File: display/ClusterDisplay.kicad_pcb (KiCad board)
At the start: 4 copper layers, 105 x 106 mm, 76 parts, among them J1 Verdin iMX95, J10 RTC coin cell, J2 Power in, J3 CAN to ECU, J4 DM-TFTR50-413 panel, J8 JTAG debug, J9 Buttons, Q1 NFET diode, Q2 NFET pass, Q3 MFT6N2A5S23A (AEC-Q101, 60V/2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, U1 LM74930-Q1, U2 LM61460-Q1, U3 TLV767-Q1, U4 TCAN1044V-Q1, U6 TPS60403-Q1, U7 AL8853AQ

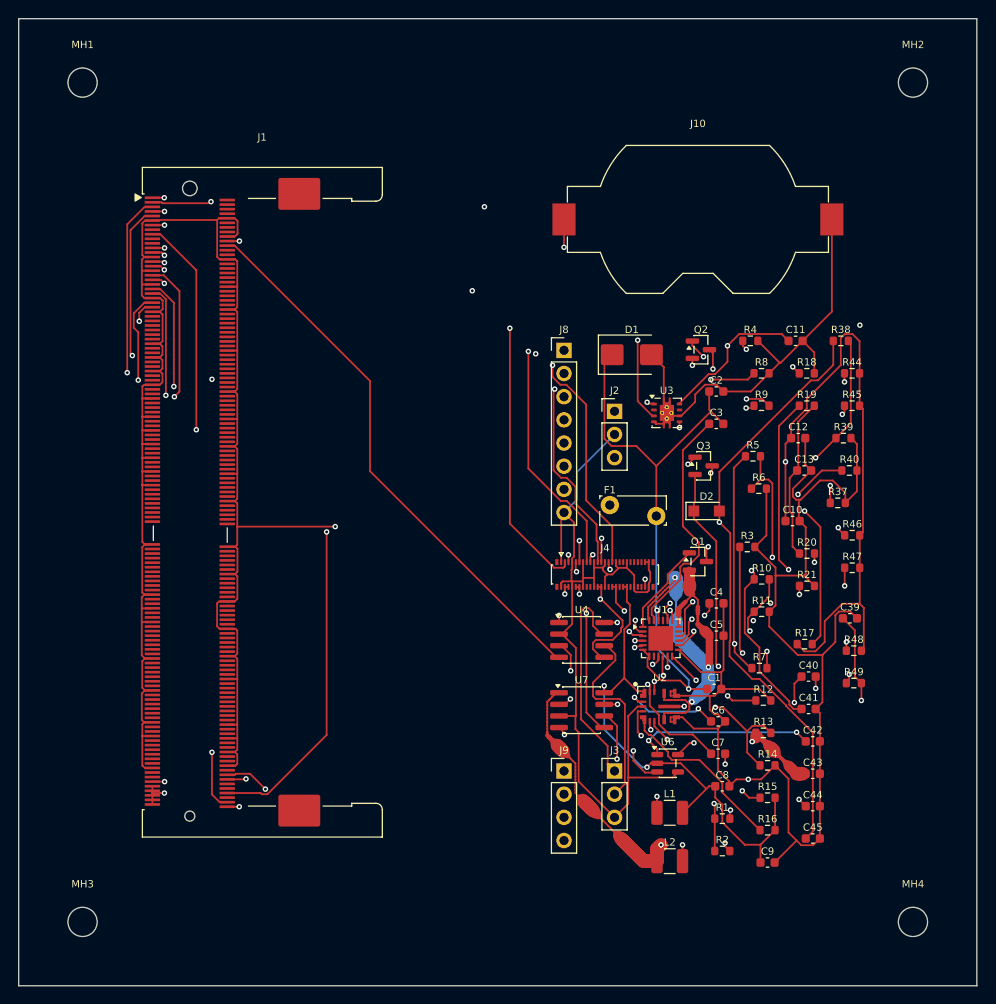
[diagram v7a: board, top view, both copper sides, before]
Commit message: display: resolve 5 of 9 TBD BOM lines with real, cited parts
Real part selection, each one researched and verified against its own
real datasheet rather than guessed:

- Q1/Q2 (front-end back-to-back FET pair): Nexperia PMV55ENEA (60V,
  VGS +-20V, 3.1A, SOT-23, AEC-Q101). Selected directly against
  LM74930-Q1's own datasheet (SNOSDF6) "MOSFET Q2 Selection" section,
  which states two real requirements: 60V VDS (matching this board's
  real single-TVS front end) and >=15V VGS rating (HGATE/DGATE can
  drive up to 14V) - PMV55ENEA satisfies both with real margin.
  Honestly flagged: its 3.1A continuous rating sits below F1's own 5A
  hold current; real steady-state current draw hasn't been
  independently verified against its SOA curve.
- D1 (input TVS): SMCJ33A - the same real part gauges/'s own front end
  already uses for the identical role.
- F1 (input fuse): Bourns MF-RG500, replacing MF-RG300. Real, not
  cosmetic: MF-RG300 (this board's footprint until now) is genuinely a
  3.0A-hold part per Bourns' own real datasheet, while the circuit's
  own target was 5A - MF-RG500 is the correct family member, with its
  own real (larger) physical package, confirmed against KiCad's
  bundled Fuse_Bourns_MF-RG500 footprint.
- J1 (Verdin SoM): real, confirmed-orderable Toradex product name
  "Verdin iMX95 Hexa 8GB WB IT" (independently listed on Mouser US and
  UK) - Hexa/8GB for real Android Automotive headroom, IT to match
  every other automotive-grade part on this board. Toradex's own
  internal order code still needs confirming at purchase time.

Regenerated schematic -> PCB -> re-routed (0 unrouted, confirmed by
real DRC via route_board.py's own new verification step) -> BOM.
Board size essentially unchanged (105.0x106.0 -> 104.8x106.0mm).

Remaining open: J2/J3/J8/J9, 4 provisional pin-header connectors -
genuinely can't be picked without knowing the real harness/enclosure
design, left open deliberately rather than guessed at.

Co-Authored-By: Claude Sonnet 5 <nore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
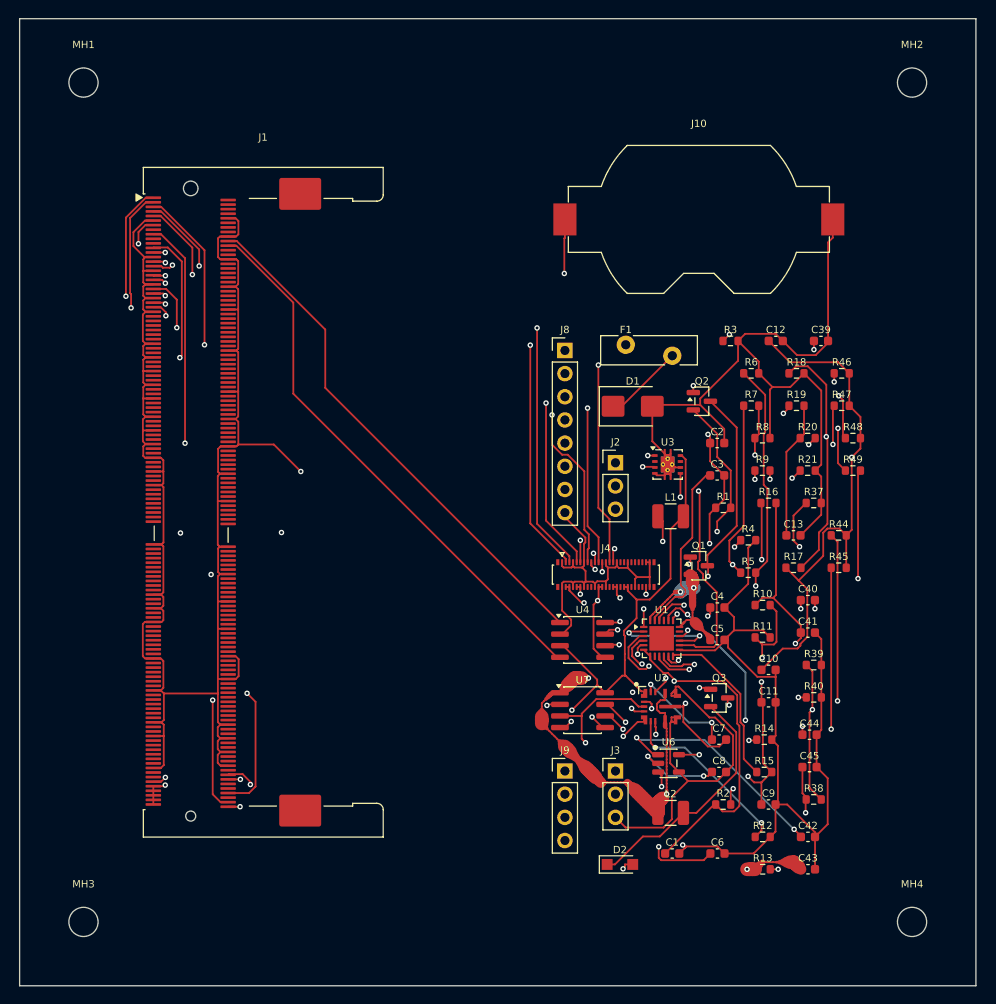
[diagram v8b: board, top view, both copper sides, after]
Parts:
- D1: value TVS 33V -> SMCJ33A
- F1: value 5A -> MF-RG500 (Bourns, 5.0A hold/8.5A trip, AEC-Q200); footprint Fuse:Fuse_Bourns_MF-RG300 -> Fuse:Fuse_Bourns_MF-RG500
- J1: value Verdin iMX95 -> Verdin iMX95 Hexa 8GB WB IT
- Q1: value NFET diode -> PMV55ENEA (AEC-Q101, 60V/20V VGS) diode
- Q2: value NFET pass -> PMV55ENEA (AEC-Q101, 60V/20V VGS) pass
- moved R38 50.4 mm to (244.6, 181.1)
- moved D2 39.9 mm to (223.4, 188.2)
- moved C11 39.7 mm to (239.7, 170.4)
- moved R16 35.9 mm to (239.7, 148.6)
- moved R1 34.1 mm to (234.7, 149.1)
- moved L1 32.5 mm to (228.9, 150.0)
- moved C39 30.6 mm to (245.4, 130.8)
- moved R7 28.8 mm to (237.8, 137.9)
- moved Q3 25.5 mm to (234.3, 169.9)
- moved R40 25.2 mm to (244.6, 169.9)
- moved R39 25.1 mm to (244.6, 166.3)
- moved R48 23.3 mm to (248.9, 141.5)
- moved R49 23.3 mm to (248.9, 145.0)
- moved R3 22.7 mm to (235.5, 130.8)
- moved R4 21.9 mm to (237.4, 152.7)
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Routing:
- net +5V: track 209.5 -> 166.7 mm, vias 6 -> 7
- net VBACKUP: track 91.4 -> 126.5 mm, vias 2 -> 3
- net SENSE_OUT: track 62.6 -> 27.7 mm, vias 4 -> 2
- net VBACKUP_CELL: track 78.9 -> 52.0 mm, vias 3 -> 2
- net ILIM: track 22.3 -> 46.8 mm
- net IMON: track 44.0 -> 20.1 mm
- net CAN1_H: track 73.2 -> 50.4 mm, vias 1 -> 2
- net PANEL_BL_LEDA_38V: track 85.1 -> 63.1 mm, vias 2 -> 3
- net +12V_PROT: track 111.1 -> 89.4 mm
- net PG_5V: track 19.6 -> 38.8 mm, vias 0 -> 3
- net BL_SW: track 45.4 -> 26.7 mm, vias 2 -> 0
- net JTAG_VREF: track 107.2 -> 89.5 mm
- net UVLO_DIV: track 55.6 -> 38.4 mm, vias 3 -> 2
- net CS_PLUS: track 43.0 -> 27.4 mm
- net +1V8: track 125.1 -> 110.4 mm
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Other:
- board size 105 x 106 mm -> 104.8 x 106 mm
